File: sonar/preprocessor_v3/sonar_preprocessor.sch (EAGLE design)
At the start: 149 parts, among them CON4 MOLEX_5566-2, U1 TEENSY_3.1_BASIC, U10 LT1117-5, U11 MMBT3904, U14 AD8336ACPZ-R7, U15 AD8336ACPZ-R7, U16 AD8336ACPZ-R7, U17 ISL21080DIH309Z-TK, U2 LTC6242, U3 MCP1501, U4 AP7331-20WG-7SOT-5, U5 MCP1501, U6 LTC6241, U8 LT3471', U9 LT1175, X1 BN35N61, X2 BN35N61, X3 BN35N61

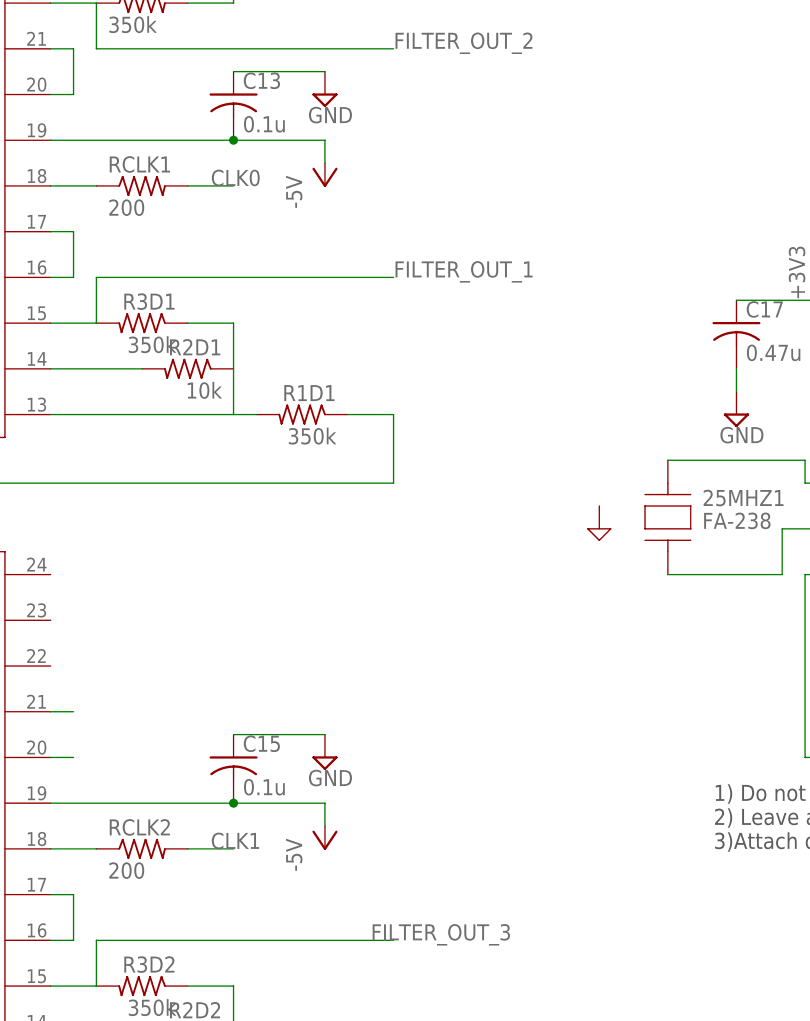
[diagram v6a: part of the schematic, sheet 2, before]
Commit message: reworked filter and clock routing
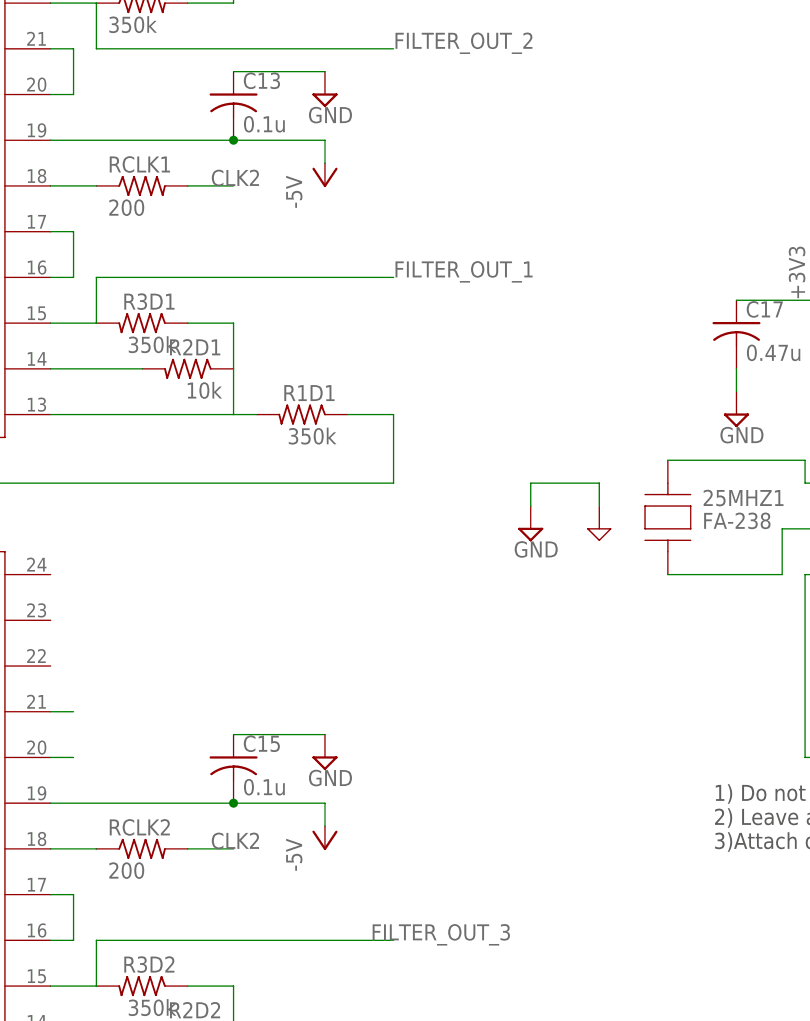
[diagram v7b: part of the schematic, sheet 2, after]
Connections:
- net CLK0: no longer RCLK1.2
- net CLK1: no longer RCLK2.2
- net CLK2: now also RCLK1.2, RCLK2.2
- net GND: now also 25MHZ1.GND
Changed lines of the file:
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@@
 <part name="SUPPLY24" library="supply2" library_urn="urn:adsk.eagle:library:372" deviceset="GND" device=""/>
 <part name="SUPPLY36" library="supply2" library_urn="urn:adsk.eagle:library:372" deviceset="V+" device=""/>
+<part name="SUPPLY37" library="supply2" library_urn="urn:adsk.eagle:library:372" deviceset="GND" device=""/>
 </parts>
 <sheets>
@@
 <instance part="+3V3" gate="G$1" x="182.88" y="119.38"/>
 <instance part="+3V4" gate="G$1" x="223.52" y="119.38"/>
+<instance part="SUPPLY37" gate="GND" x="149.86" y="88.9"/>
 </instances>
 <busses>
@@
 <label x="213.36" y="93.98" size="1.778" layer="95"/>
 </segment>
-<segment>
-<pinref part="RCLK2" gate="G$1" pin="2"/>
-<wire x1="111.76" y1="53.34" x2="116.84" y2="53.34" width="0.1524" layer="91"/>
-<label x="114.3" y="53.34" size="1.778" layer="95"/>
-</segment>
 </net>
 <net name="+5V" class="0">
@@
 <wire x1="228.6" y1="104.14" x2="228.6" y2="106.68" width="0.1524" layer="91"/>
 </segment>
+<segment>
+<pinref part="SUPPLY37" gate="GND" pin="GND"/>
+<wire x1="149.86" y1="91.44" x2="149.86" y2="93.98" width="0.1524" layer="91"/>
+<pinref part="25MHZ1" gate="G$1" pin="GND"/>
+<wire x1="149.86" y1="93.98" x2="157.48" y2="93.98" width="0.1524" layer="91"/>
+<wire x1="157.48" y1="93.98" x2="157.48" y2="91.44" width="0.1524" layer="91"/>
+</segment>
 </net>
 <net name="-5V" class="0">
@@
 <label x="213.36" y="78.74" size="1.778" layer="95"/>
 </segment>
+<segment>
+<pinref part="RCLK1" gate="G$1" pin="2"/>
+<wire x1="111.76" y1="127" x2="116.84" y2="127" width="0.1524" layer="91"/>
+<label x="114.3" y="127" size="1.778" layer="95"/>
+</segment>
+<segment>
+<pinref part="RCLK2" gate="G$1" pin="2"/>
+<wire x1="111.76" y1="53.34" x2="116.84" y2="53.34" width="0.1524" layer="91"/>
+<label x="114.3" y="53.34" size="1.778" layer="95"/>
+</segment>
 </net>
 <net name="CLK0" class="0">
@@
 <label x="213.36" y="99.06" size="1.778" layer="95"/>
 </segment>
-<segment>
-<pinref part="RCLK1" gate="G$1" pin="2"/>
-<wire x1="111.76" y1="127" x2="116.84" y2="127" width="0.1524" layer="91"/>
-<label x="114.3" y="127" size="1.778" layer="95"/>
-</segment>
-</net>
+</net>

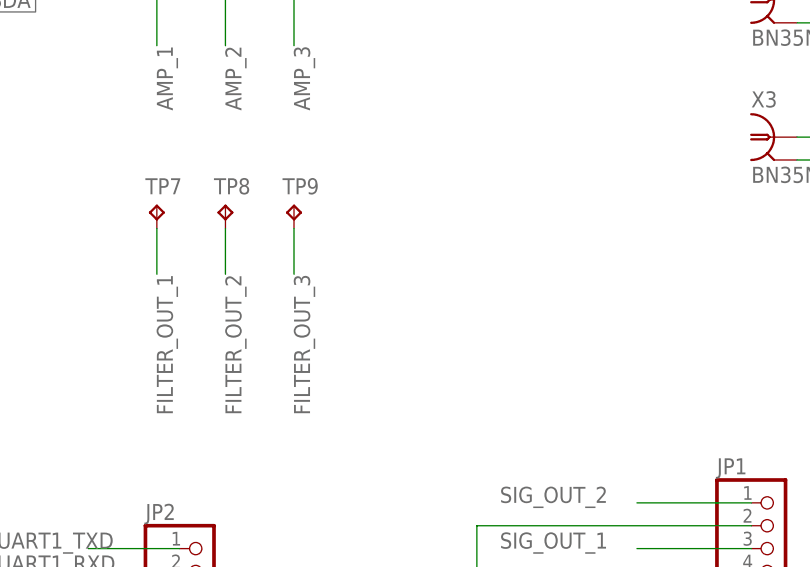
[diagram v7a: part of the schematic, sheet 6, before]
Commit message: added silk screen text and ground vias
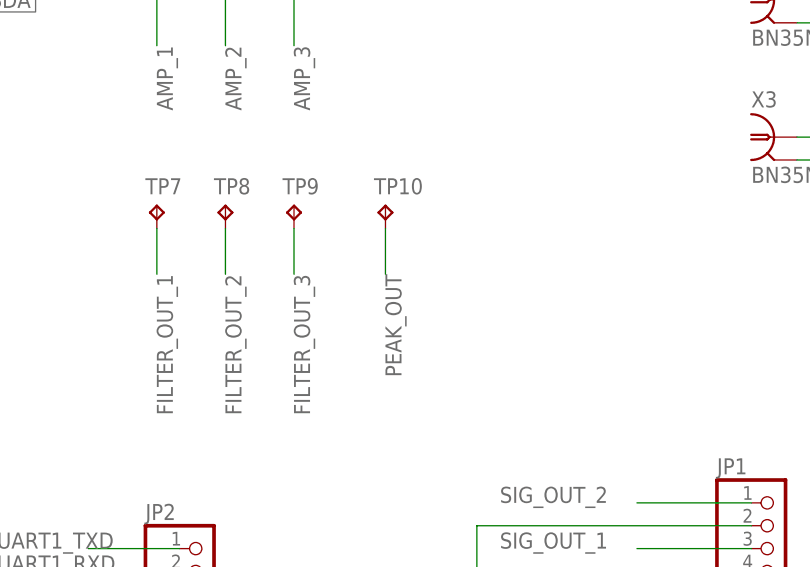
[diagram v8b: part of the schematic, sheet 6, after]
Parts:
- added TP10: TPB2,54, testpad:TPB2,54
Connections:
- net PEAK_OUT: now also TP10.TP
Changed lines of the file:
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@@
 <part name="SUPPLY36" library="supply2" library_urn="urn:adsk.eagle:library:372" deviceset="V+" device=""/>
 <part name="SUPPLY37" library="supply2" library_urn="urn:adsk.eagle:library:372" deviceset="GND" device=""/>
+<part name="TP10" library="testpad" library_urn="urn:adsk.eagle:library:385" deviceset="TP" device="B2,54" package3d_urn="urn:adsk.eagle:package:27948/1"/>
 </parts>
 <sheets>
@@
 <instance part="SUPPLY24" gate="GND" x="137.16" y="17.78"/>
 <instance part="SUPPLY36" gate="1" x="27.94" y="48.26"/>
+<instance part="TP10" gate="G$1" x="167.64" y="104.14"/>
 </instances>
 <busses>
@@
 <label x="78.74" y="154.94" size="1.778" layer="95"/>
 </segment>
-</net>
+<segment>
+<pinref part="TP10" gate="G$1" pin="TP"/>
+<wire x1="167.64" y1="101.6" x2="167.64" y2="96.52" width="0.1524" layer="91"/>
+<label x="167.64" y="96.52" size="1.778" layer="95" rot="R270"/>
+</segment>
+</net>
